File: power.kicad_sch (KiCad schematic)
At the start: 30 parts, among them J2 KYCO-P4S-S, J3 MicroFit_2x02, J3B1 DNI, J4 DC 24V/5A OUT, Q1 BC847, Q2 IRF9540SPBF, SW1 DNI, U1 MAX5035BUSA, U6 MC78M12BDTG

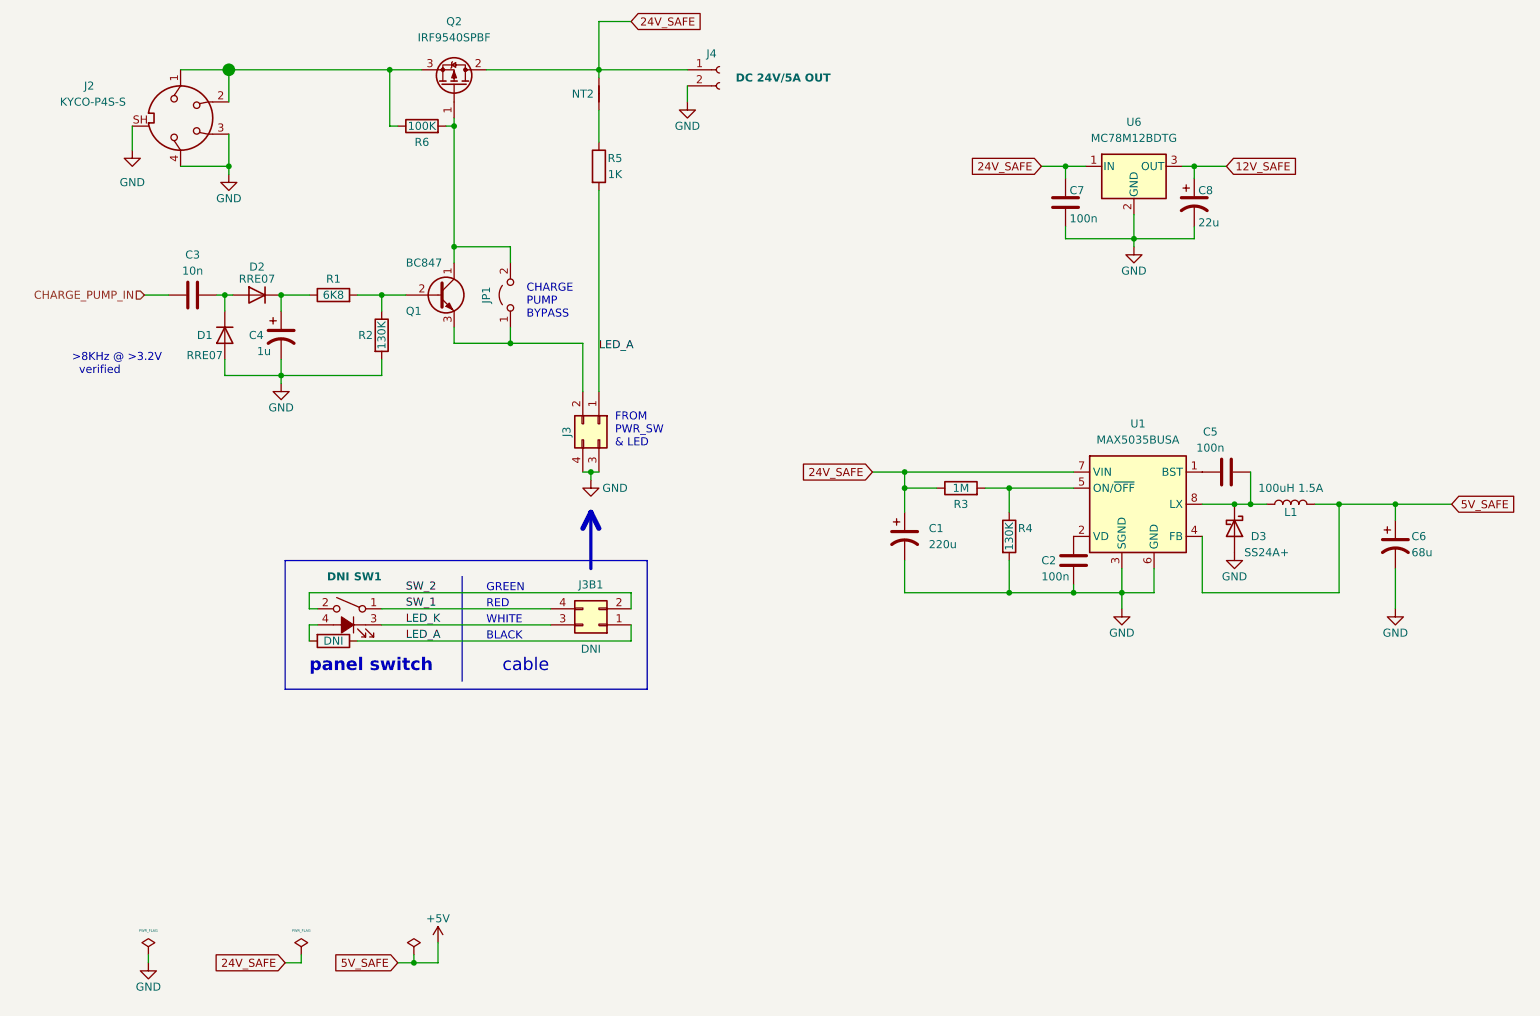
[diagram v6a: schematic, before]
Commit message: Scary file corruption turns out to be just bugs in eschema.
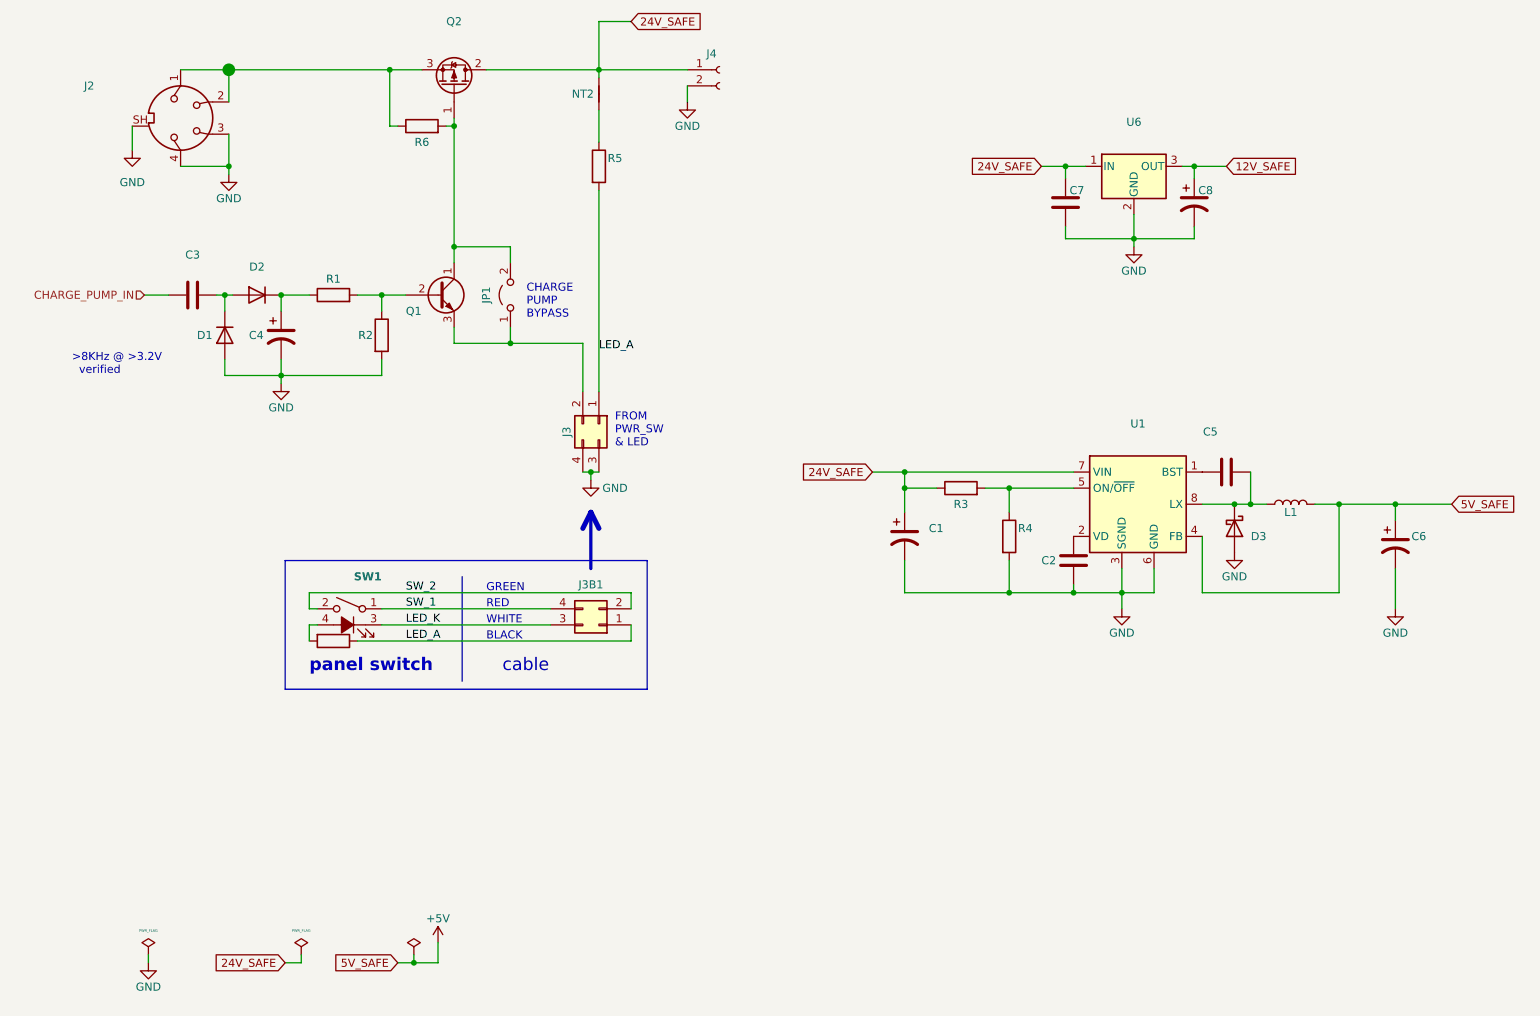
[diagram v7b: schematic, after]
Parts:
- C1: value 220u -> (none)
- C2, C5, C7: value 100n -> (none)
- C3: value 10n -> (none)
- C4: value 1u -> (none)
- C6: value 68u -> (none)
- C8: value 22u -> (none)
- D1, D2: value RRE07 -> (none)
- D3: value SS24A+ -> (none)
- J2: value KYCO-P4S-S -> (none)
- J3: value MicroFit_2x02 -> (none)
- J3B1, NT2, R101, SW1: value DNI -> (none)
- J4: value DC 24V/5A OUT -> (none)
- JP1: value Jumper_2_Bridged -> (none)
- L1: value 100uH 1.5A -> (none)
- Q1: value BC847 -> (none)
- Q2: value IRF9540SPBF -> (none)
- R1: value 6K8 -> (none)
- R2, R4: value 130K -> (none)
- R3: value 1M -> (none)
- R5: value 1K -> (none)
- R6: value 100K -> (none)
- U1: value MAX5035BUSA -> (none)
- U6: value MC78M12BDTG -> (none)
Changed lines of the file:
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@@
     (in_bom yes) (on_board yes)
     (property "Reference" "D3" (id 0) (at 209.55 102.87 90))
-    (property "Value" "SS24A+" (id 1) (at 210.82 105.41 90))
+    (property "Value" "" (id 1) (at 210.82 105.41 90))
     (property "Footprint" "" (id 2) (at 205.74 101.6 0)
       (effects (font (size 1.27 1.27)) hide)
@@
       (effects (font (size 1.27 1.27) bold) (justify left))
     )
-    (property "Value" "DNI" (id 1) (at 66.04 109.22 0)
+    (property "Value" "" (id 1) (at 66.04 109.22 0)
       (effects (font (size 1.27 1.27) bold) (justify left))
     )
@@
     (in_bom yes) (on_board yes)
     (property "Reference" "R1" (id 0) (at 63.5 62.23 90))
-    (property "Value" "6K8" (id 1) (at 63.5 64.77 90))
+    (property "Value" "" (id 1) (at 63.5 64.77 90))
     (property "Footprint" "" (id 2) (at 63.5 66.548 90)
       (effects (font (size 1.27 1.27)) hide)
@@
       (effects (font (size 1.27 1.27)) (justify left))
     )
-    (property "Value" "22u" (id 1) (at 200.025 53.34 0)
+    (property "Value" "" (id 1) (at 200.025 53.34 0)
       (effects (font (size 1.27 1.27)) (justify left))
     )
@@
       (effects (font (size 1.27 1.27)) (justify left))
     )
-    (property "Value" "BC847" (id 1) (at 74.93 59.69 0)
+    (property "Value" "" (id 1) (at 74.93 59.69 0)
       (effects (font (size 1.27 1.27)) (justify left))
     )
@@
     (in_bom yes) (on_board yes)
     (property "Reference" "C5" (id 0) (at 201.93 86.36 90))
-    (property "Value" "100n" (id 1) (at 201.93 88.9 90))
+    (property "Value" "" (id 1) (at 201.93 88.9 90))
     (property "Footprint" "" (id 2) (at 208.28 91.7448 0)
       (effects (font (size 1.27 1.27)) hide)
@@
     (in_bom yes) (on_board yes)
     (property "Reference" "R6" (id 0) (at 77.47 40.64 90))
-    (property "Value" "100K" (id 1) (at 77.47 38.1 90))
+    (property "Value" "" (id 1) (at 77.47 38.1 90))
     (property "Footprint" "" (id 2) (at 77.47 39.878 90)
       (effects (font (size 1.27 1.27)) hide)
@@
     (in_bom yes) (on_board yes)
     (property "Reference" "NT2" (id 0) (at 102.87 33.02 90))
-    (property "Value" "DNI" (id 1) (at 107.95 33.02 0)
+    (property "Value" "" (id 1) (at 107.95 33.02 0)
       (effects (font (size 1.27 1.27)) hide)
     )
@@
     (in_bom yes) (on_board yes)
     (property "Reference" "R3" (id 0) (at 162.56 97.79 90))
-    (property "Value" "1M" (id 1) (at 162.56 95.25 90))
+    (property "Value" "" (id 1) (at 162.56 95.25 90))
     (property "Footprint" "" (id 2) (at 162.56 97.028 90)
       (effects (font (size 1.27 1.27)) hide)
@@
     (in_bom yes) (on_board yes)
     (property "Reference" "JP1" (id 0) (at 87.63 64.77 0))
-    (property "Value" "Jumper_2_Bridged" (id 1) (at 92.71 66.0399 90)
+    (property "Value" "" (id 1) (at 92.71 66.0399 90)
       (effects (font (size 1.27 1.27)) (justify right) hide)
     )
@@
       (effects (font (size 1.27 1.27)) (justify left))
     )
-    (property "Value" "220u" (id 1) (at 157.48 104.14 0)
+    (property "Value" "" (id 1) (at 157.48 104.14 0)
       (effects (font (size 1.27 1.27)) (justify left))
     )
@@
     (in_bom yes) (on_board yes)
     (property "Reference" "C3" (id 0) (at 41.275 58.42 90))
-    (property "Value" "10n" (id 1) (at 41.275 60.96 90))
+    (property "Value" "" (id 1) (at 41.275 60.96 90))
     (property "Footprint" "" (id 2) (at 45.085 63.8048 0)
       (effects (font (size 1.27 1.27)) hide)
@@
     (in_bom yes) (on_board yes)
     (property "Reference" "R4" (id 0) (at 172.72 101.6 0))
-    (property "Value" "130K" (id 1) (at 170.18 102.87 90))
+    (property "Value" "" (id 1) (at 170.18 102.87 90))
     (property "Footprint" "" (id 2) (at 168.402 102.87 90)
       (effects (font (size 1.27 1.27)) hide)
@@
     (in_bom yes) (on_board yes) (fields_autoplaced)
     (property "Reference" "U1" (id 0) (at 190.5 85.09 0))
-    (property "Value" "MAX5035BUSA" (id 1) (at 190.5 87.63 0))
+    (property "Value" "" (id 1) (at 190.5 87.63 0))
     (property "Footprint" "" (id 2) (at 194.31 106.68 0)
       (effects (font (size 1.27 1.27) italic) (justify left) hide)
@@
       (effects (font (size 1.27 1.27)) (justify left))
     )
-    (property "Value" "KYCO-P4S-S" (id 1) (at 20.32 34.29 90)
+    (property "Value" "" (id 1) (at 20.32 34.29 90)
       (effects (font (size 1.27 1.27)) (justify left))
     )
@@
     (in_bom yes) (on_board yes)
     (property "Reference" "J4" (id 0) (at 123.19 26.67 0))
-    (property "Value" "DC 24V/5A OUT" (id 1) (at 127 30.48 0)
+    (property "Value" "" (id 1) (at 127 30.48 0)
       (effects (font (size 1.27 1.27) bold) (justify left))
     )
@@
     (in_bom yes) (on_board yes)
     (property "Reference" "R5" (id 0) (at 107.95 43.18 0))
-    (property "Value" "1K" (id 1) (at 107.95 45.72 0))
+    (property "Value" "" (id 1) (at 107.95 45.72 0))
     (property "Footprint" "" (id 2) (at 103.632 44.45 90)
       (effects (font (size 1.27 1.27)) hide)
@@
     (in_bom yes) (on_board yes)
     (property "Reference" "R2" (id 0) (at 68.58 71.12 0))
-    (property "Value" "130K" (id 1) (at 71.12 71.12 90))
+    (property "Value" "" (id 1) (at 71.12 71.12 90))
     (property "Footprint" "" (id 2) (at 69.342 71.12 90)
       (effects (font (size 1.27 1.27)) hide)
@@
     (in_bom yes) (on_board yes)
     (property "Reference" "D1" (id 0) (at 43.18 71.12 90))
-    (property "Value" "RRE07" (id 1) (at 43.18 74.295 90))
+    (property "Value" "" (id 1) (at 43.18 74.295 90))
     (property "Footprint" "" (id 2) (at 46.355 71.12 0)
       (effects (font (size 1.27 1.27)) hide)
@@
       (effects (font (size 1.27 1.27)) hide)
     )
-    (property "Value" "DNI" (id 1) (at 63.5 119.38 90))
+    (property "Value" "" (id 1) (at 63.5 119.38 90))
     (property "Footprint" "" (id 2) (at 63.5 117.602 90)
       (effects (font (size 1.27 1.27)) hide)
@@
       (effects (font (size 1.27 1.27)) (justify left))
     )
-    (property "Value" "68u" (id 1) (at 233.68 105.41 0)
+    (property "Value" "" (id 1) (at 233.68 105.41 0)
       (effects (font (size 1.27 1.27)) (justify left))
     )
@@
       (effects (font (size 1.27 1.27)) (justify left))
     )
-    (property "Value" "1u" (id 1) (at 51.435 73.66 0)
+    (property "Value" "" (id 1) (at 51.435 73.66 0)
       (effects (font (size 1.27 1.27)) (justify left))
     )
@@
     (in_bom yes) (on_board yes) (fields_autoplaced)
     (property "Reference" "Q2" (id 0) (at 82.55 21.59 90))
-    (property "Value" "IRF9540SPBF" (id 1) (at 82.55 24.13 90))
+    (property "Value" "" (id 1) (at 82.55 24.13 90))
     (property "Footprint" "" (id 2) (at 85.09 26.67 0)
       (effects (font (size 1.27 1.27)) hide)
@@
       (effects (font (size 1.27 1.27)) (justify left))
     )
-    (property "Value" "100n" (id 1) (at 179.705 52.705 0)
+    (property "Value" "" (id 1) (at 179.705 52.705 0)
       (effects (font (size 1.27 1.27)) (justify left))
     )
@@
     (in_bom yes) (on_board yes)
     (property "Reference" "J3" (id 0) (at 100.33 86.36 0))
-    (property "Value" "MicroFit_2x02" (id 1) (at 107.95 83.82 0)
+    (property "Value" "" (id 1) (at 107.95 83.82 0)
       (effects (font (size 1.27 1.27)) hide)
     )
@@
     (in_bom no) (on_board no)
     (property "Reference" "J3B1" (id 0) (at 104.14 110.49 0))
-    (property "Value" "DNI" (id 1) (at 104.14 120.65 0))
+    (property "Value" "" (id 1) (at 104.14 120.65 0))
     (property "Footprint" "" (id 2) (at 105.41 116.84 0)
       (effects (font (size 1.27 1.27)) hide)
@@
       (effects (font (size 1.27 1.27)) (justify left))
     )
-    (property "Value" "100n" (id 1) (at 175.26 109.22 0)
+    (property "Value" "" (id 1) (at 175.26 109.22 0)
       (effects (font (size 1.27 1.27)) (justify left))
     )
@@
     (in_bom yes) (on_board yes)
     (property "Reference" "D2" (id 0) (at 51.435 60.325 0))
-    (property "Value" "RRE07" (id 1) (at 51.435 62.23 0))
+    (property "Value" "" (id 1) (at 51.435 62.23 0))
     (property "Footprint" "" (id 2) (at 51.435 64.77 0)
       (effects (font (size 1.27 1.27)) hide)
@@
     (in_bom yes) (on_board yes) (fields_autoplaced)
     (property "Reference" "U6" (id 0) (at 189.865 37.465 0))
-    (property "Value" "MC78M12BDTG" (id 1) (at 189.865 40.005 0))
+    (property "Value" "" (id 1) (at 189.865 40.005 0))
     (property "Footprint" "" (id 2) (at 190.5 48.26 0)
       (effects (font (size 1.27 1.27) italic) (justify left) hide)
@@
     (in_bom yes) (on_board yes)
     (property "Reference" "L1" (id 0) (at 214.63 99.06 90))
-    (property "Value" "100uH 1.5A" (id 1) (at 214.63 95.25 90))
+    (property "Value" "" (id 1) (at 214.63 95.25 90))
     (property "Footprint" "" (id 2) (at 214.63 97.79 0)
       (effects (font (size 1.27 1.27)) hide)

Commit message: Removed 'Element14' field from all sch/pcb components
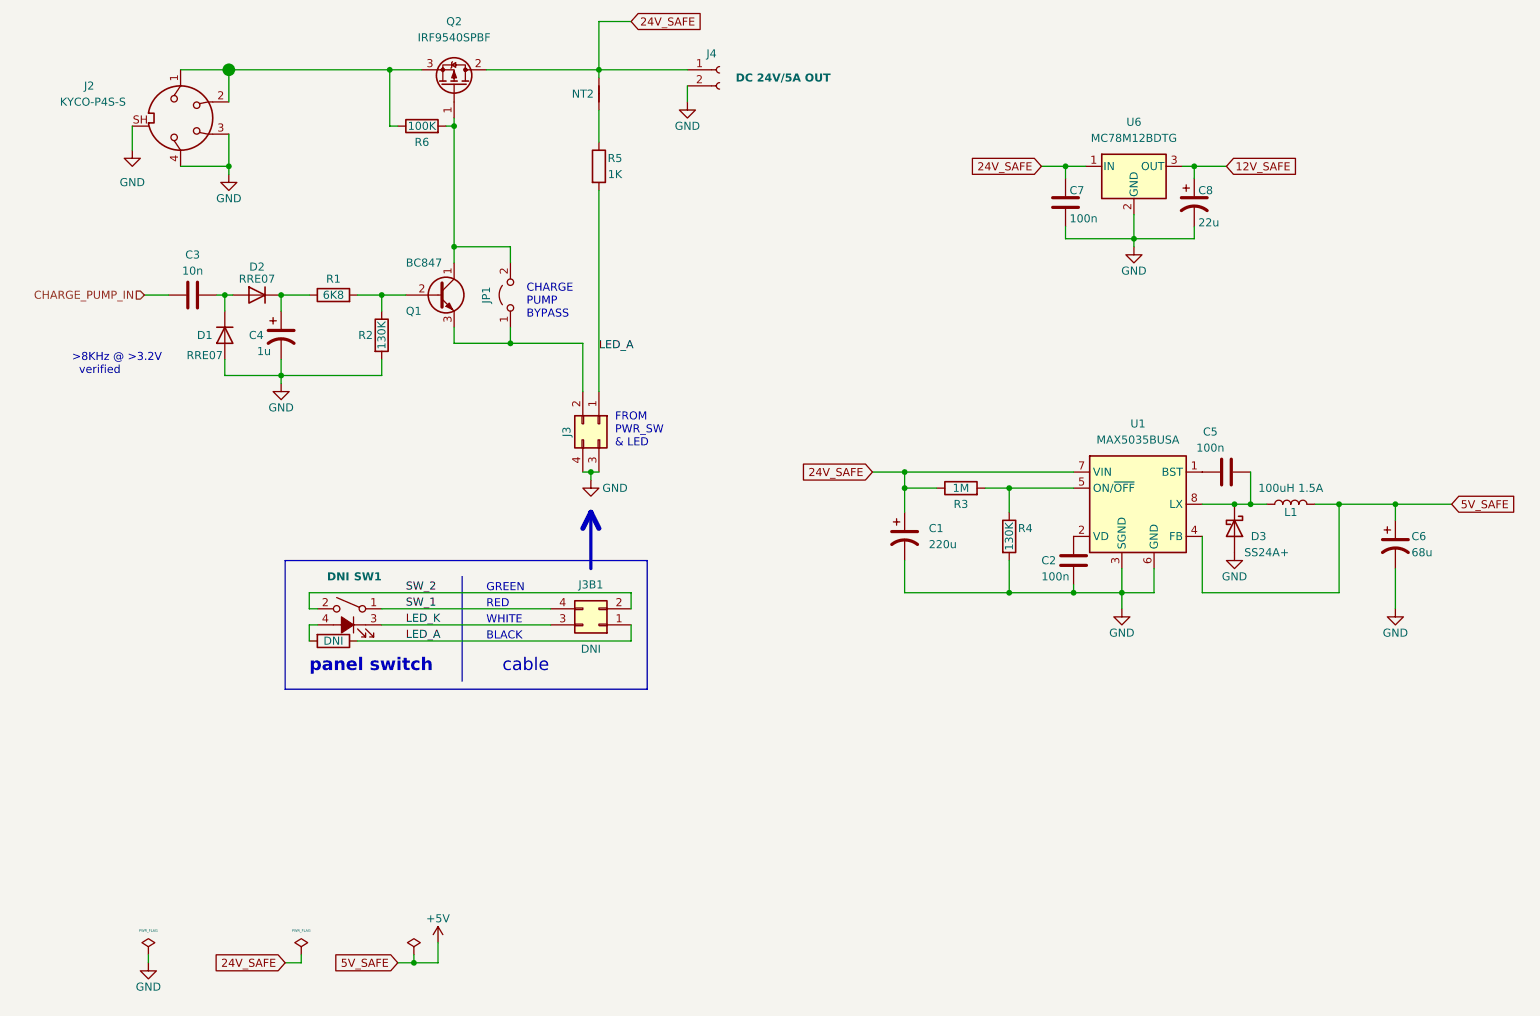
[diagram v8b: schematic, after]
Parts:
- C1: value (none) -> 220u; footprint (none) -> Capacitor_SMD:CP_Elec_8x10.5
- C2, C5, C7: value (none) -> 100n; footprint (none) -> Capacitor_SMD:C_0603_1608Metric
- C3: value (none) -> 10n; footprint (none) -> Capacitor_SMD:C_0603_1608Metric
- C4: value (none) -> 1u; footprint (none) -> Capacitor_SMD:C_0603_1608Metric
- C6: value (none) -> 68u; footprint (none) -> Capacitor_SMD:CP_Elec_6.3x7.7
- C8: value (none) -> 22u; footprint (none) -> Capacitor_SMD:C_0603_1608Metric
- D1, D2: value (none) -> RRE07; footprint (none) -> Diode_SMD:D_SOD-323_HandSoldering
- D3: value (none) -> SS24A+; footprint (none) -> Diode_SMD:D_SMA
- J2: value (none) -> KYCO-P4S-S; footprint (none) -> _footprints:KYCON_KPJX-4S-S
- J3: value (none) -> MicroFit_2x02; footprint (none) -> Connector_Molex:Molex_Micro-Fit_3.0_43045-0412_2x02_P3.00mm_Vertical
- J3B1, R101, SW1: value (none) -> DNI
- J4: value (none) -> DC 24V/5A OUT; footprint (none) -> TerminalBlock_RND:TerminalBlock_RND_205-00232_1x02_P5.08mm_Horizontal
- JP1: value (none) -> Jumper_2_Bridged; footprint (none) -> Connector_PinHeader_2.54mm:PinHeader_2x01_P2.54mm_Vertical
- L1: value (none) -> 100uH 1.5A; footprint (none) -> Inductor_SMD:L_12x12mm_H6mm
- NT2: value (none) -> DNI; footprint (none) -> _footprints:NetTie-2_SMD_Pad0.3mm
- Q1: value (none) -> BC847; footprint (none) -> Package_TO_SOT_SMD:SOT-23
- Q2: value (none) -> IRF9540SPBF; footprint (none) -> Package_TO_SOT_SMD:TO-263-2
- R1: value (none) -> 6K8; footprint (none) -> Resistor_SMD:R_0603_1608Metric
- R2, R4: value (none) -> 130K; footprint (none) -> Resistor_SMD:R_0603_1608Metric
- R3: value (none) -> 1M; footprint (none) -> Resistor_SMD:R_0603_1608Metric
- R5: value (none) -> 1K; footprint (none) -> Resistor_SMD:R_0603_1608Metric
- R6: value (none) -> 100K; footprint (none) -> Resistor_SMD:R_0603_1608Metric
- U1: value (none) -> MAX5035BUSA; footprint (none) -> Package_SO:SOIC-8_3.9x4.9mm_P1.27mm
- U6: value (none) -> MC78M12BDTG; footprint (none) -> Package_TO_SOT_SMD:TO-252-2
